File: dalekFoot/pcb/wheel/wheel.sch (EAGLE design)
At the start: 75 parts, among them IC1 LM1117MP-3.3, IC3 LM1117MP-3.3, IC4 4051D, IC5 4051D, IC6 LM1117MP-3.3, U1 TB6612FNG(O,C,8,EL, U2 SS8050-SOT-23, U3 SS8050-SOT-23, U4 SS8050-SOT-23, U5 TB6612FNG(O,C,8,EL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

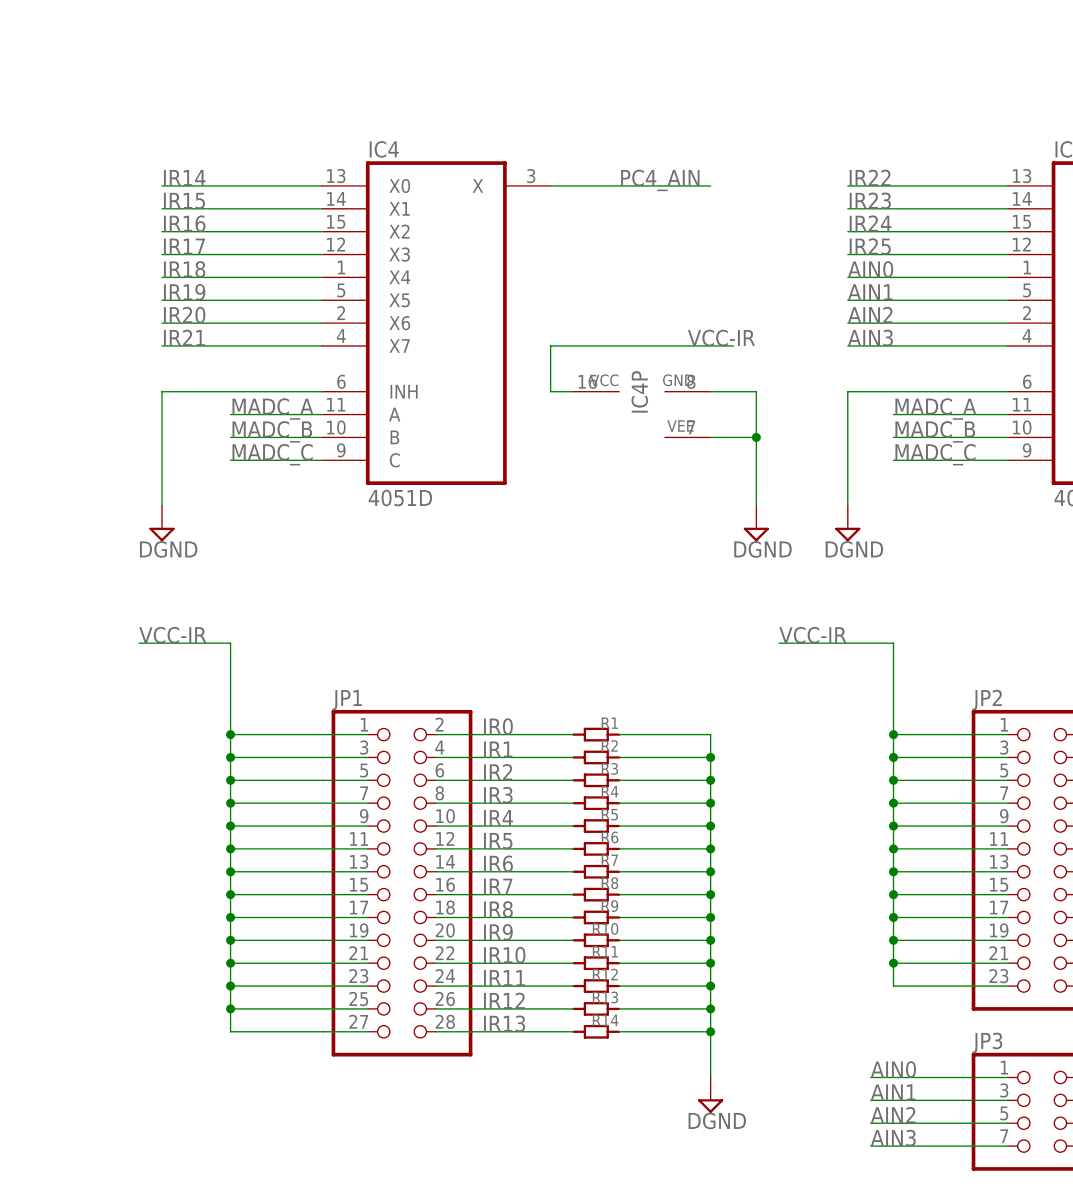
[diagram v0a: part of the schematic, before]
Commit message: routing finished, not tested
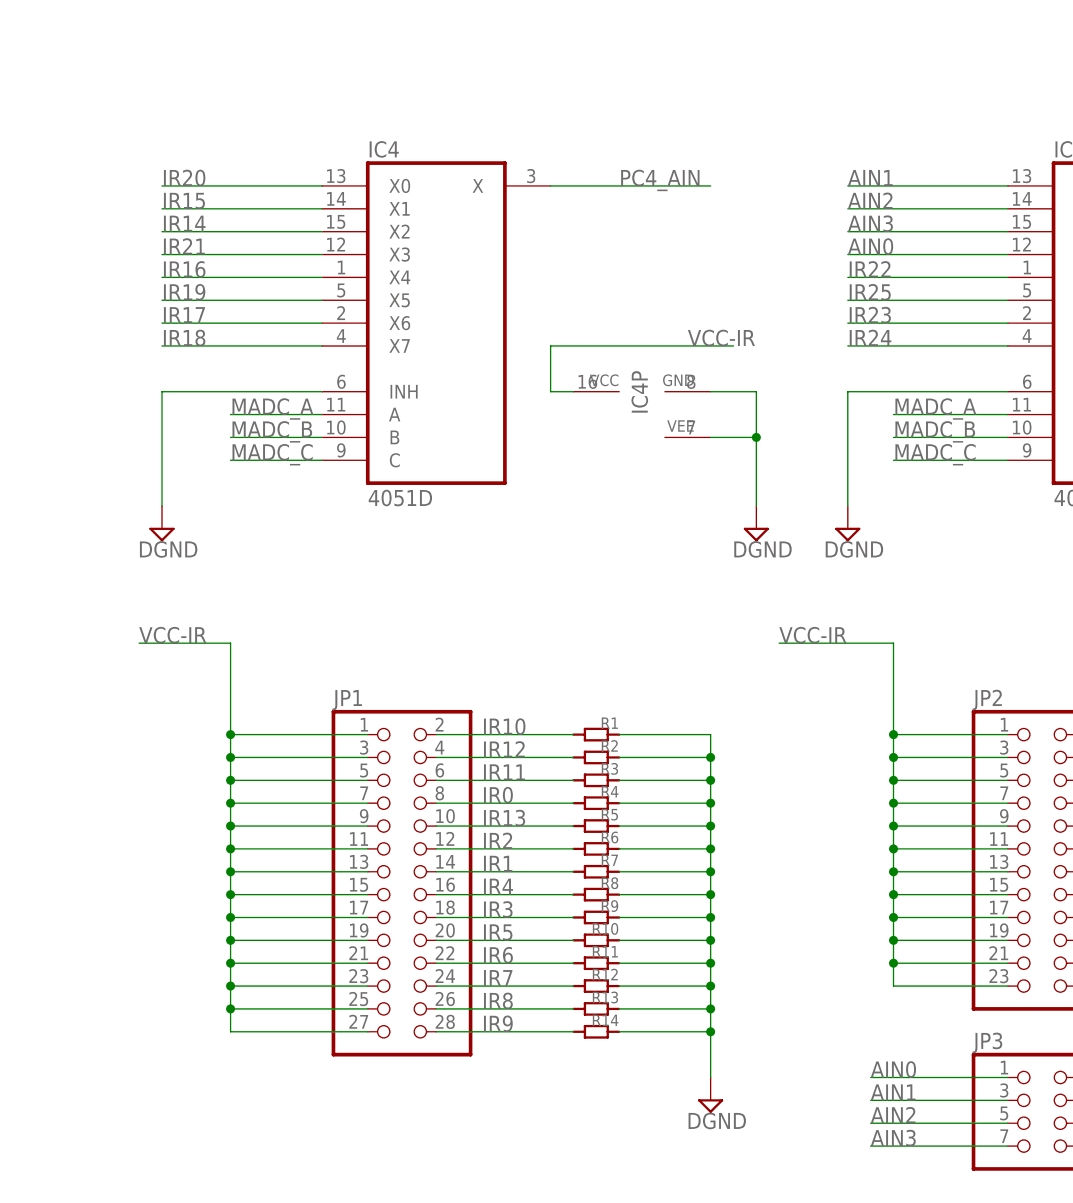
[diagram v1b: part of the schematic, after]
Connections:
- net AIN0: now also IC5A.X3; no longer IC5A.X4
- net AIN1: now also IC5A.X0; no longer IC5A.X5
- net AIN2: now also IC5A.X1; no longer IC5A.X6
- net AIN3: now also IC5A.X2; no longer IC5A.X7
- net IR0: now also JP1.8, R4.P$2; no longer JP1.2, R1.P$2
- net IR1: now also JP1.14, R7.P$2; no longer JP1.4, R2.P$2
- net IR10: now also JP1.2, R1.P$2; no longer JP1.22, R11.P$2
- net IR11: now also JP1.6, R3.P$2; no longer JP1.24, R12.P$2
- net IR12: now also JP1.4, R2.P$2; no longer JP1.26, R13.P$2
- net IR13: now also JP1.10, R5.P$2; no longer JP1.28, R14.P$2
- net IR14: now also IC4A.X2; no longer IC4A.X0
- net IR16: now also IC4A.X4; no longer IC4A.X2
- net IR17: now also IC4A.X6; no longer IC4A.X3
- net IR18: now also IC4A.X7; no longer IC4A.X4
- net IR2: now also JP1.12, R6.P$2; no longer JP1.6, R3.P$2
- net IR20: now also IC4A.X0; no longer IC4A.X6
- net IR21: now also IC4A.X3; no longer IC4A.X7
- net IR22: now also IC5A.X4; no longer IC5A.X0
- net IR23: now also IC5A.X6; no longer IC5A.X1
- net IR24: now also IC5A.X7; no longer IC5A.X2
- net IR25: now also IC5A.X5; no longer IC5A.X3
- net IR3: now also JP1.18, R9.P$2; no longer JP1.8, R4.P$2
- net IR4: now also JP1.16, R8.P$2; no longer JP1.10, R5.P$2
- net IR5: now also JP1.20, R10.P$2; no longer JP1.12, R6.P$2
- net IR6: now also JP1.22, R11.P$2; no longer JP1.14, R7.P$2
- net IR7: now also JP1.24, R12.P$2; no longer JP1.16, R8.P$2
- net IR8: now also JP1.26, R13.P$2; no longer JP1.18, R9.P$2
- net IR9: now also JP1.28, R14.P$2; no longer JP1.20, R10.P$2

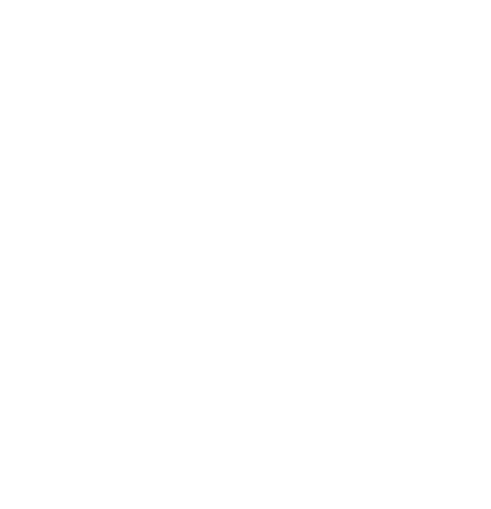
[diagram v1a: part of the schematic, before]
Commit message: add logo
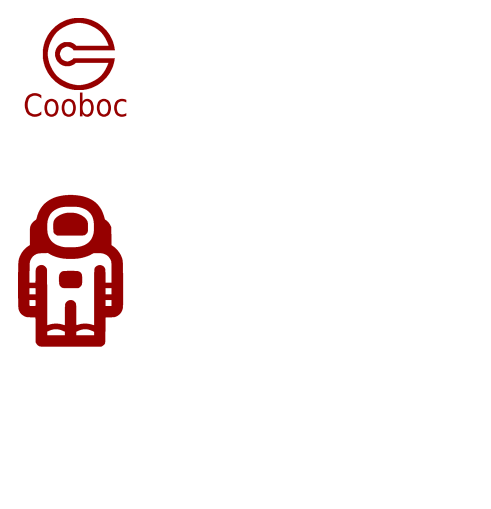
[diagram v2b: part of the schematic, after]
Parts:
- added U$3: COOBOC-PLACE, hqc-logo:COOBOC-PLACE
- added U$4: ASTRONANT, hqc-logo:ASTRONANT
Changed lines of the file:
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@@
 <part name="B3" library="switch-tact" deviceset="DTSM-6-2PIN" device=""/>
 <part name="B4" library="switch-tact" deviceset="DTSM-6-2PIN" device=""/>
+<part name="U$3" library="hqc-logo" deviceset="COOBOC-PLACE" device=""/>
+<part name="U$4" library="hqc-logo" deviceset="ASTRONANT" device=""/>
 </parts>
 <sheets>
@@
 <instance part="B3" gate="G$1" x="96.52" y="391.16" rot="R270"/>
 <instance part="B4" gate="G$1" x="121.92" y="375.92" rot="R270"/>
+<instance part="U$3" gate="G$1" x="-27.94" y="627.38"/>
+<instance part="U$4" gate="G$1" x="-35.56" y="596.9"/>
 </instances>
 <busses>

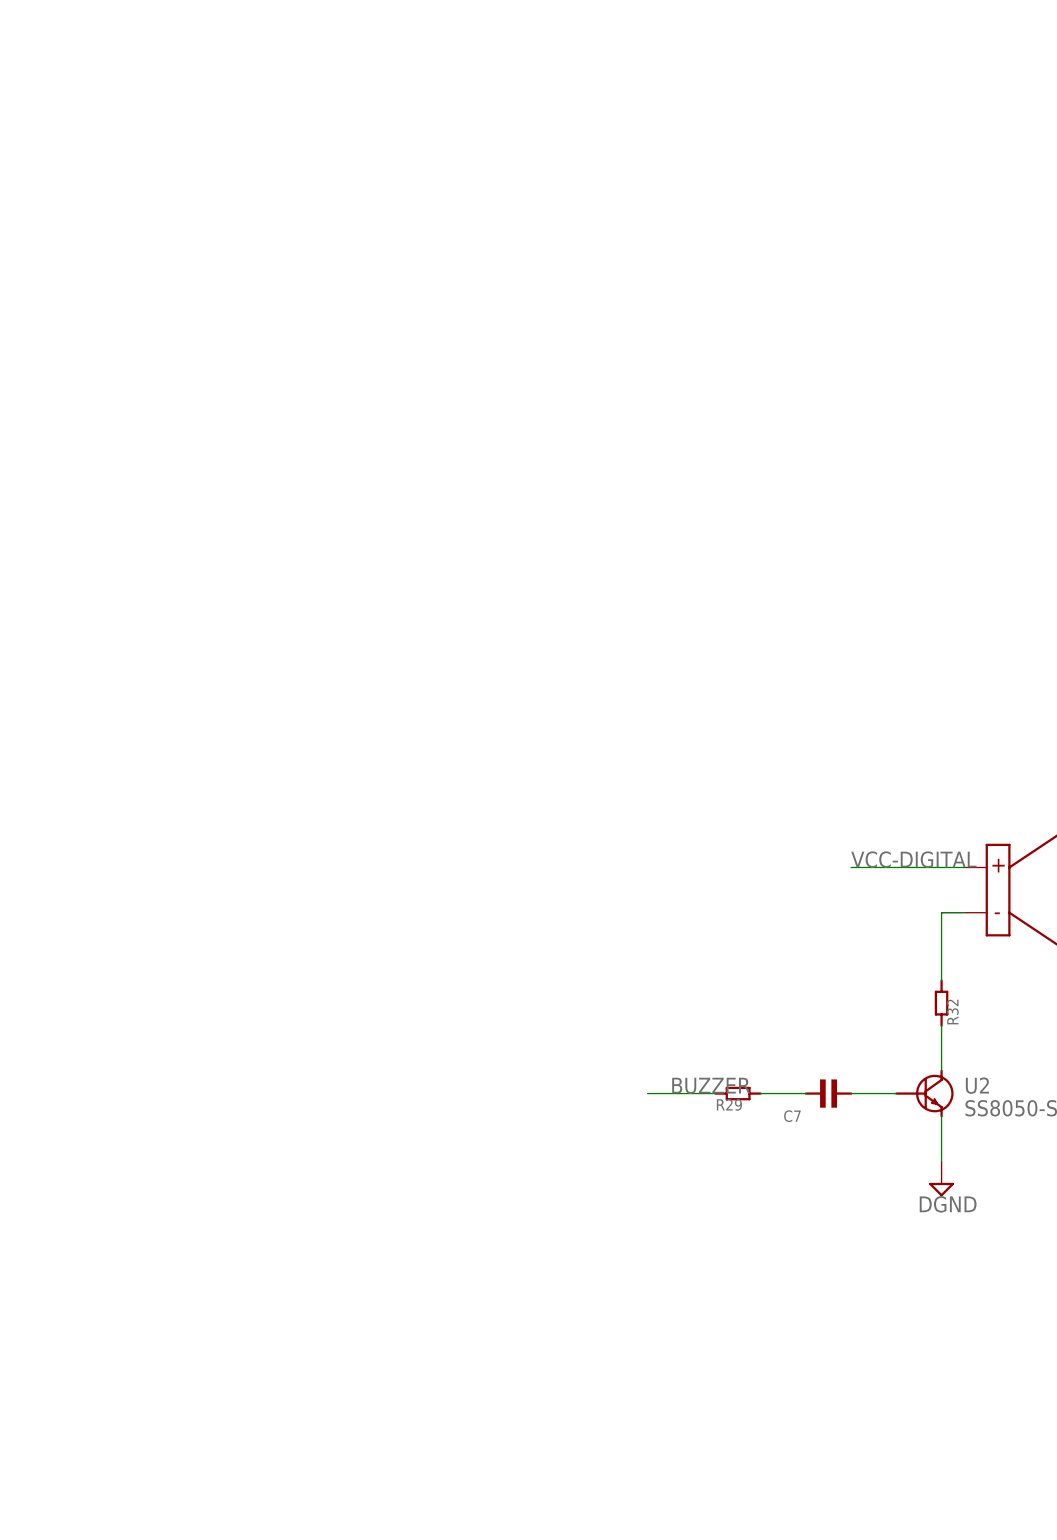
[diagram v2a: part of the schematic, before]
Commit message: Multiple bug fixed
1. add mouting holes
2. remove capacitor for buzzer
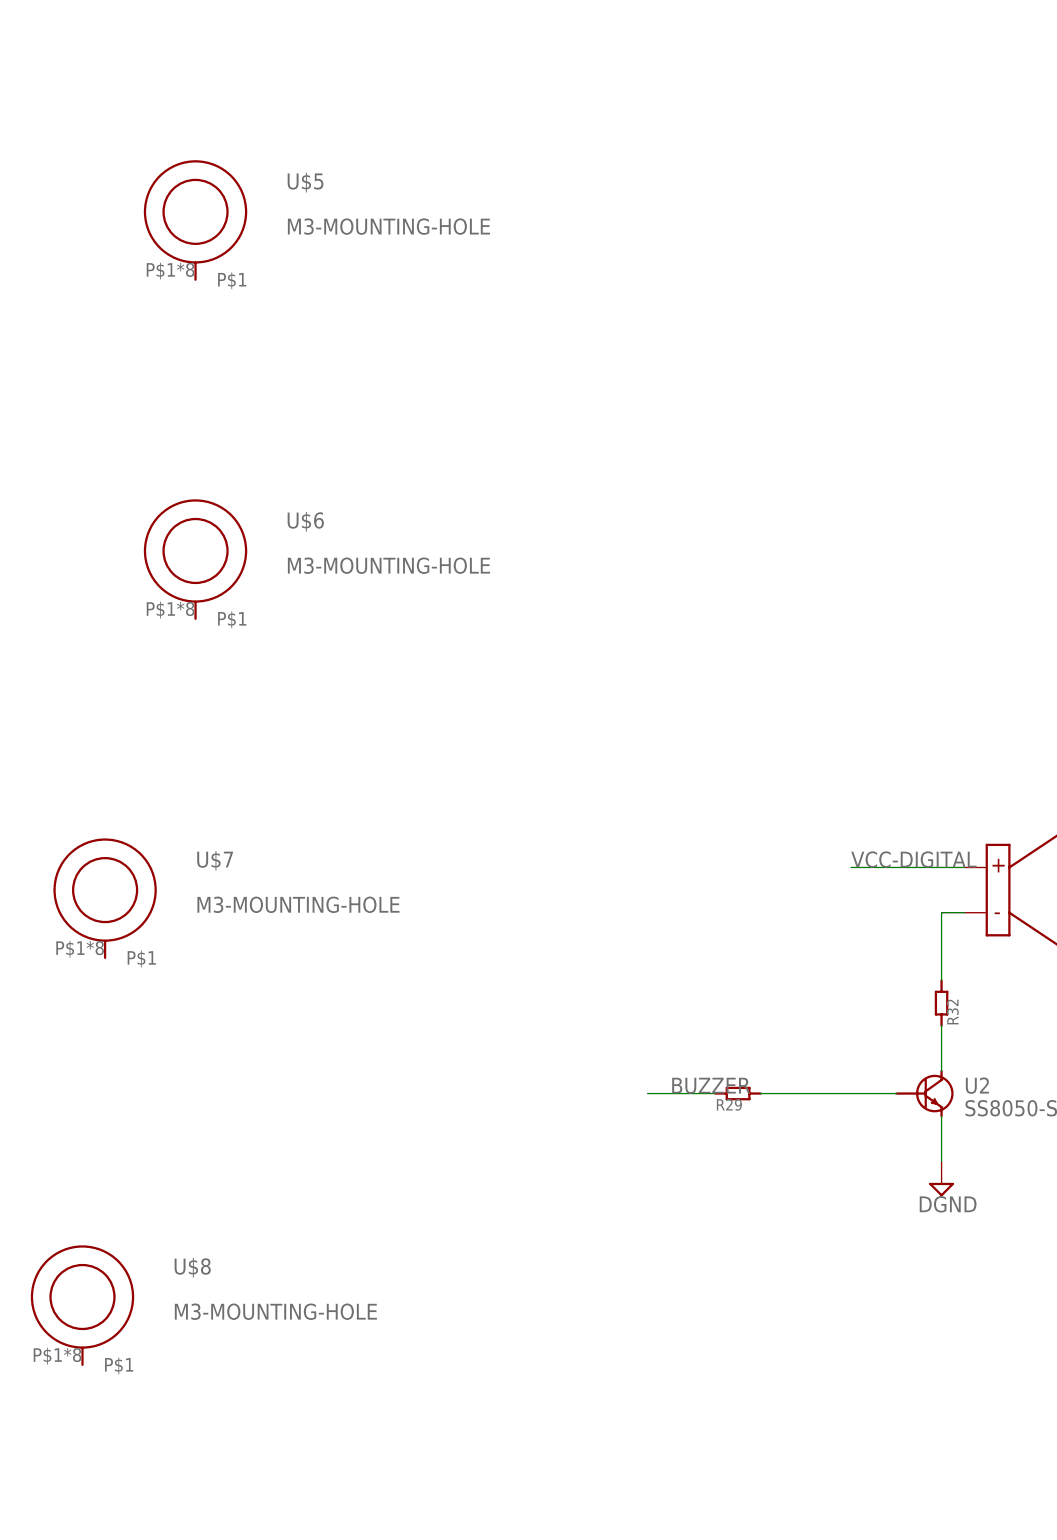
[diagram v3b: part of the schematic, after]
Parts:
- removed C7: (no value), hqc:C-0805
- added U$5, U$6, U$7, U$8: M3-MOUNTING-HOLE, hqc:M3-MOUNTING-HOLE
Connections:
- removed net N$9: C7.P$1, R29.P$2
- net N$12: now also R29.P$2; no longer C7.P$2
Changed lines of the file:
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@@
 <part name="LED1" library="led" deviceset="LED" device="CHIP-LED0805"/>
 <part name="LED2" library="led" deviceset="LED" device="CHIP-LED0805"/>
-<part name="C7" library="hqc" deviceset="C-0805" device=""/>
 <part name="U5" library="TB6612FNG" deviceset="TB6612FNG(O,C,8,EL" device=""/>
 <part name="SUPPLY28" library="supply2" deviceset="DGND" device=""/>
@@
 <part name="U$3" library="hqc-logo" deviceset="COOBOC-PLACE" device=""/>
 <part name="U$4" library="hqc-logo" deviceset="ASTRONANT" device=""/>
+<part name="U$5" library="hqc" deviceset="M3-MOUNTING-HOLE" device=""/>
+<part name="U$6" library="hqc" deviceset="M3-MOUNTING-HOLE" device=""/>
+<part name="U$7" library="hqc" deviceset="M3-MOUNTING-HOLE" device=""/>
+<part name="U$8" library="hqc" deviceset="M3-MOUNTING-HOLE" device=""/>
 </parts>
 <sheets>
@@
 <instance part="LED1" gate="G$1" x="99.06" y="454.66"/>
 <instance part="LED2" gate="G$1" x="149.86" y="454.66"/>
-<instance part="C7" gate="G$1" x="33.02" y="431.8"/>
 <instance part="U5" gate="G$1" x="160.02" y="596.9"/>
 <instance part="SUPPLY28" gate="G$1" x="180.34" y="558.8"/>
@@
 <instance part="U$3" gate="G$1" x="-27.94" y="627.38"/>
 <instance part="U$4" gate="G$1" x="-35.56" y="596.9"/>
+<instance part="U$5" gate="G$1" x="-38.1" y="530.86"/>
+<instance part="U$6" gate="G$1" x="-38.1" y="492.76"/>
+<instance part="U$7" gate="G$1" x="-48.26" y="454.66"/>
+<instance part="U$8" gate="G$1" x="-50.8" y="408.94"/>
 </instances>
 <busses>
@@
 </segment>
 </net>
-<net name="N$9" class="0">
-<segment>
+<net name="N$12" class="0">
+<segment>
+<pinref part="U2" gate="G$1" pin="P$B"/>
 <pinref part="R29" gate="G$1" pin="P$2"/>
-<pinref part="C7" gate="G$1" pin="P$1"/>
-<wire x1="25.4" y1="431.8" x2="30.48" y2="431.8" width="0.1524" layer="91"/>
-</segment>
-</net>
-<net name="N$12" class="0">
-<segment>
-<pinref part="C7" gate="G$1" pin="P$2"/>
-<pinref part="U2" gate="G$1" pin="P$B"/>
-<wire x1="35.56" y1="431.8" x2="40.64" y2="431.8" width="0.1524" layer="91"/>
-</segment>
-</net>
+<wire x1="40.64" y1="431.8" x2="25.4" y2="431.8" width="0.1524" layer="91"/>
+</segment>
+</net>
